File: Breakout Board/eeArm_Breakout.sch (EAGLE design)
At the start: 21 parts, among them X1 ESP8266

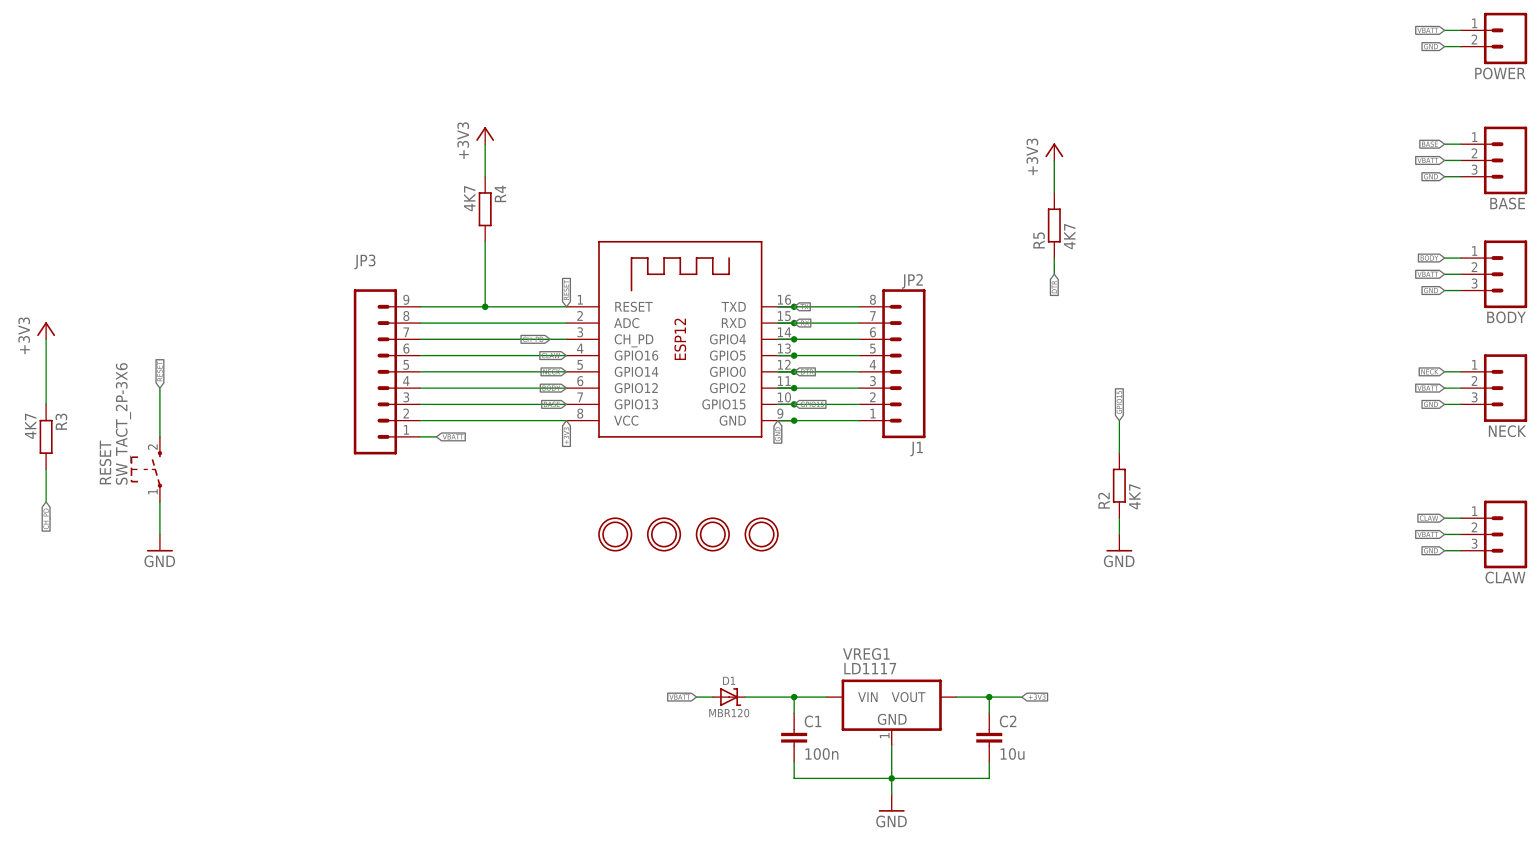
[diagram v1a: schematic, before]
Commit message: Ready for panelising
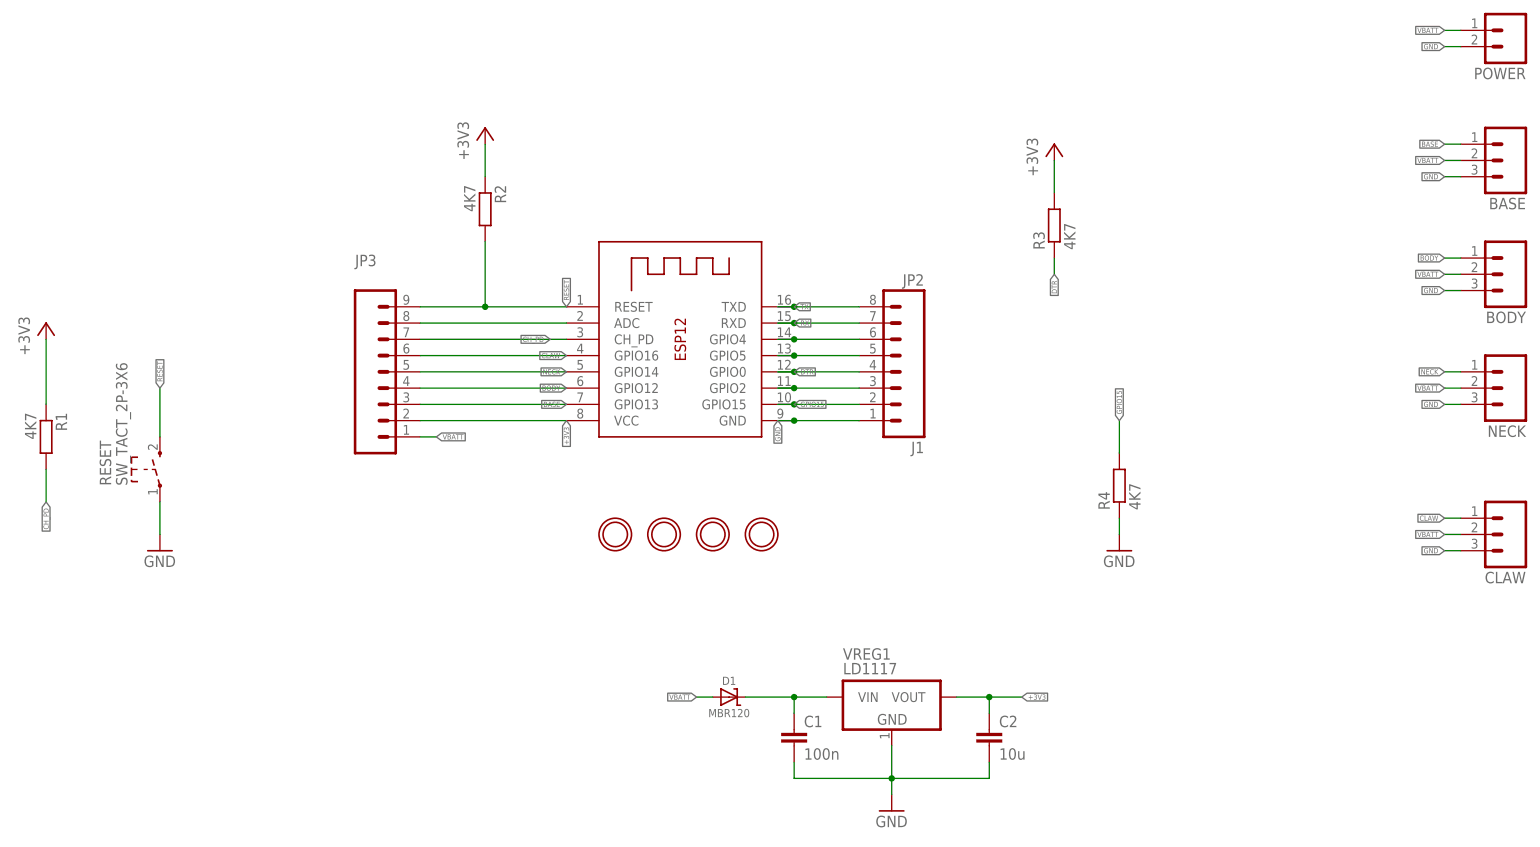
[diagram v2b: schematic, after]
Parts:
- removed R5: 4K7, resistor:R-EU_R0805
- added R1: 4K7, resistor:R-EU_R0805
- added U$1: MAKERSPACE_LOGO, Gwa's Parts:MAKERSPACE_LOGO
- X1: device microbuilder:ESP-12 -> Gwa's Parts:ESP-12X
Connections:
- net +3V3: now also R1.1, R2.1, R3.2; no longer R3.1, R4.1, R5.2
- net CH_PD: now also R1.2; no longer R3.2
- net DTR: now also R3.1; no longer R5.1
- net GND: now also R4.1; no longer R2.1
- net GPIO15: now also R4.2; no longer R2.2
- net RESET: now also R2.2; no longer R4.2
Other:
- moved on the sheet: R2, R3, R4
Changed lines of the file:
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@@
 </classes>
 <parts>
-<part name="R3" library="resistor" deviceset="R-EU_" device="R0805" value="4K7"/>
+<part name="R1" library="resistor" deviceset="R-EU_" device="R0805" value="4K7"/>
 <part name="+3V4" library="supply1" deviceset="+3V3" device=""/>
 <part name="JP2" library="SparkFun-Connectors" deviceset="M08" device="LOCK" value="J1"/>
 <part name="C1" library="resistor" deviceset="C-EU" device="C0805" value="100n"/>
+<part name="R2" library="resistor" deviceset="R-EU_" device="R0805" value="4K7"/>
+<part name="+3V2" library="supply1" deviceset="+3V3" device=""/>
+<part name="R3" library="resistor" deviceset="R-EU_" device="R0805" value="4K7"/>
+<part name="+3V5" library="supply1" deviceset="+3V3" device=""/>
 <part name="R4" library="resistor" deviceset="R-EU_" device="R0805" value="4K7"/>
-<part name="+3V2" library="supply1" deviceset="+3V3" device=""/>
-<part name="R5" library="resistor" deviceset="R-EU_" device="R0805" value="4K7"/>
-<part name="+3V5" library="supply1" deviceset="+3V3" device=""/>
-<part name="R2" library="resistor" deviceset="R-EU_" device="R0805" value="4K7"/>
 <part name="RESET" library="Gwa's Parts" deviceset="SW_TACT_2P" device="-3X6"/>
 <part name="VREG1" library="dp_devices" deviceset="VREG_3PINS" device="-SOT-223" value="LD1117"/>
 <part name="C2" library="resistor" deviceset="C-EU" device="C0805" value="10u"/>
 <part name="D1" library="microbuilder" deviceset="DIODE-SCHOTTKY" device="SOD-123" value="MBR120"/>
-<part name="X1" library="microbuilder" deviceset="ESP-12" device="" value="ESP8266"/>
+<part name="X1" library="Gwa's Parts" deviceset="ESP-12" device="X" value="ESP8266"/>
 <part name="GND1" library="supply1" deviceset="GND" device=""/>
 <part name="GND4" library="supply1" deviceset="GND" device=""/>
@@
 <part name="U$9" library="microbuilder" deviceset="MOUNTINGHOLE" device="2.0"/>
 <part name="JP3" library="SparkFun-Connectors" deviceset="M09" device="LOCK"/>
+<part name="U$1" library="Gwa's Parts" deviceset="MAKERSPACE_LOGO" device=""/>
 </parts>
 <sheets>
@@
 </plain>
 <instances>
-<instance part="R3" gate="G$1" x="-38.1" y="48.26" rot="R270"/>
+<instance part="R1" gate="G$1" x="-38.1" y="48.26" rot="R270"/>
 <instance part="+3V4" gate="G$1" x="-38.1" y="66.04"/>
 <instance part="JP2" gate="G$1" x="93.98" y="58.42" rot="MR0"/>
 <instance part="C1" gate="G$1" x="78.74" y="2.54"/>
-<instance part="R4" gate="G$1" x="30.48" y="83.82" rot="R270"/>
+<instance part="R2" gate="G$1" x="30.48" y="83.82" rot="R270"/>
 <instance part="+3V2" gate="G$1" x="30.48" y="96.52"/>
-<instance part="R5" gate="G$1" x="119.38" y="81.28" rot="R90"/>
+<instance part="R3" gate="G$1" x="119.38" y="81.28" rot="R90"/>
 <instance part="+3V5" gate="G$1" x="119.38" y="93.98"/>
-<instance part="R2" gate="G$1" x="129.54" y="40.64" rot="R90"/>
+<instance part="R4" gate="G$1" x="129.54" y="40.64" rot="R90"/>
 <instance part="RESET" gate="SW" x="-20.32" y="43.18" rot="R90"/>
 <instance part="VREG1" gate="VREG" x="93.98" y="7.62"/>
@@
 <instance part="U$9" gate="G$1" x="73.66" y="33.02"/>
 <instance part="JP3" gate="G$1" x="10.16" y="58.42"/>
+<instance part="U$1" gate="G$1" x="160.02" y="5.08"/>
 </instances>
 <busses>
@@
 </segment>
 <segment>
-<pinref part="R2" gate="G$1" pin="1"/>
+<pinref part="R4" gate="G$1" pin="1"/>
 <wire x1="129.54" y1="35.56" x2="129.54" y2="33.02" width="0.1524" layer="91"/>
 <pinref part="GND5" gate="1" pin="GND"/>
@@
 <segment>
 <pinref part="+3V4" gate="G$1" pin="+3V3"/>
-<pinref part="R3" gate="G$1" pin="1"/>
+<pinref part="R1" gate="G$1" pin="1"/>
 <wire x1="-38.1" y1="53.34" x2="-38.1" y2="63.5" width="0.1524" layer="91"/>
 </segment>
 <segment>
-<pinref part="R4" gate="G$1" pin="1"/>
+<pinref part="R2" gate="G$1" pin="1"/>
 <pinref part="+3V2" gate="G$1" pin="+3V3"/>
 <wire x1="30.48" y1="88.9" x2="30.48" y2="93.98" width="0.1524" layer="91"/>
 </segment>
 <segment>
-<pinref part="R5" gate="G$1" pin="2"/>
+<pinref part="R3" gate="G$1" pin="2"/>
 <pinref part="+3V5" gate="G$1" pin="+3V3"/>
 <wire x1="119.38" y1="86.36" x2="119.38" y2="91.44" width="0.1524" layer="91"/>
@@
 </segment>
 <segment>
-<pinref part="R5" gate="G$1" pin="1"/>
+<pinref part="R3" gate="G$1" pin="1"/>
 <wire x1="119.38" y1="76.2" x2="119.38" y2="73.66" width="0.1524" layer="91"/>
 <label x="119.38" y="73.66" size="0.8128" layer="95" rot="R270" xref="yes"/>
@@
 </segment>
 <segment>
-<pinref part="R2" gate="G$1" pin="2"/>
+<pinref part="R4" gate="G$1" pin="2"/>
 <wire x1="129.54" y1="45.72" x2="129.54" y2="50.8" width="0.1524" layer="91"/>
 <label x="129.54" y="50.8" size="0.8128" layer="95" rot="R90" xref="yes"/>
@@
 </segment>
 <segment>
-<pinref part="R3" gate="G$1" pin="2"/>
+<pinref part="R1" gate="G$1" pin="2"/>
 <wire x1="-38.1" y1="43.18" x2="-38.1" y2="38.1" width="0.1524" layer="91"/>
 <label x="-38.1" y="38.1" size="0.8128" layer="95" rot="R270" xref="yes"/>
@@
 <segment>
 <wire x1="43.18" y1="68.58" x2="30.48" y2="68.58" width="0.1524" layer="91"/>
-<pinref part="R4" gate="G$1" pin="2"/>
+<pinref part="R2" gate="G$1" pin="2"/>
 <wire x1="30.48" y1="68.58" x2="20.32" y2="68.58" width="0.1524" layer="91"/>
 <wire x1="30.48" y1="78.74" x2="30.48" y2="68.58" width="0.1524" layer="91"/>

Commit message: Go time
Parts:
- removed U$1: MAKERSPACE_LOGO, Gwa's Parts:MAKERSPACE_LOGO
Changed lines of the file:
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@@
 <?xml version="1.0" encoding="utf-8"?>
 <!DOCTYPE eagle SYSTEM "eagle.dtd">
-<eagle version="7.3.0">
+<eagle version="7.2.0">
 <drawing>
 <settings>
@@
 <part name="U$9" library="microbuilder" deviceset="MOUNTINGHOLE" device="2.0"/>
 <part name="JP3" library="SparkFun-Connectors" deviceset="M09" device="LOCK"/>
-<part name="U$1" library="Gwa's Parts" deviceset="MAKERSPACE_LOGO" device=""/>
 </parts>
 <sheets>
@@
 <instance part="U$9" gate="G$1" x="73.66" y="33.02"/>
 <instance part="JP3" gate="G$1" x="10.16" y="58.42"/>
-<instance part="U$1" gate="G$1" x="160.02" y="5.08"/>
 </instances>
 <busses>
